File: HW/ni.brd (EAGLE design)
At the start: 122.5 x 35 mm, 71 parts, among them IC1 FAN3100TSX, IC2 STM32G071CBU6, IC3 MIC5504-3.3YM5-TR, Q1 FQD12N20L, Q10 CPH3461, Q11 CPH3461, Q12 CPH3461, Q13 BF821SMD, Q14 CPH3461, Q15 BF821SMD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

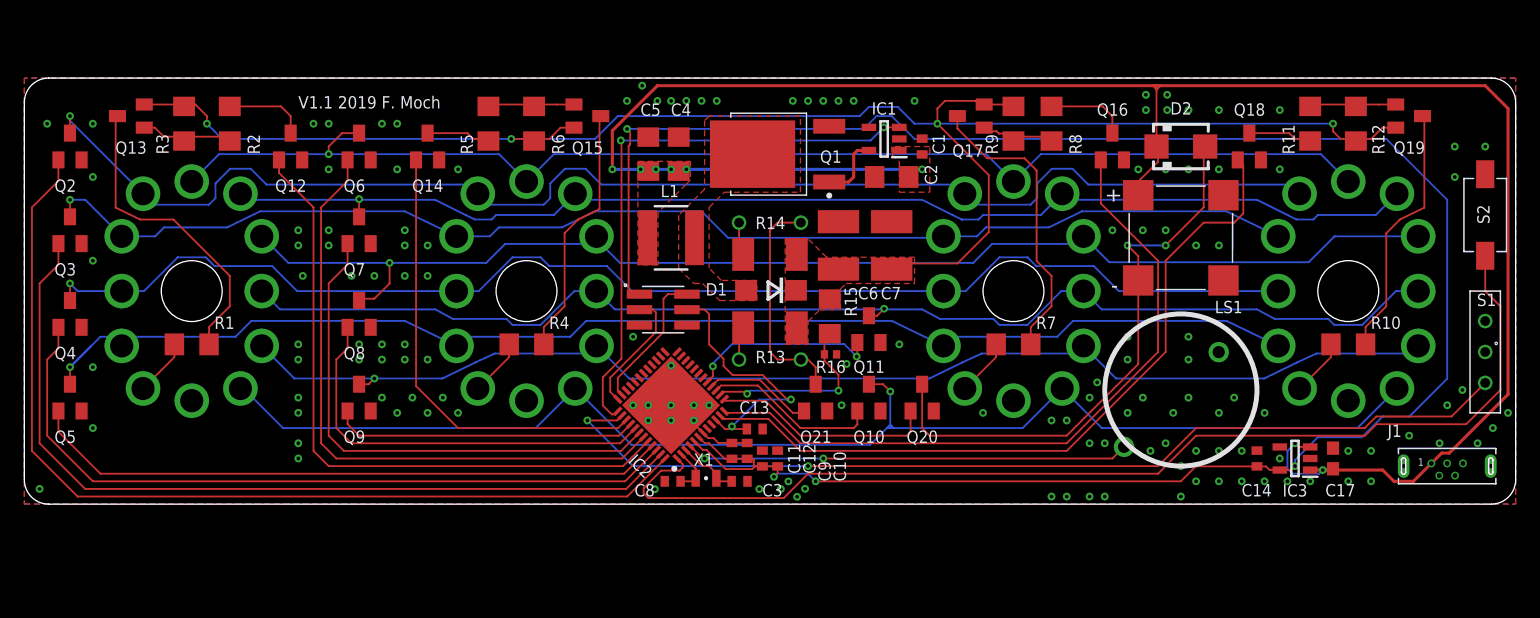
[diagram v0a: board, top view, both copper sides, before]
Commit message: WIFI added
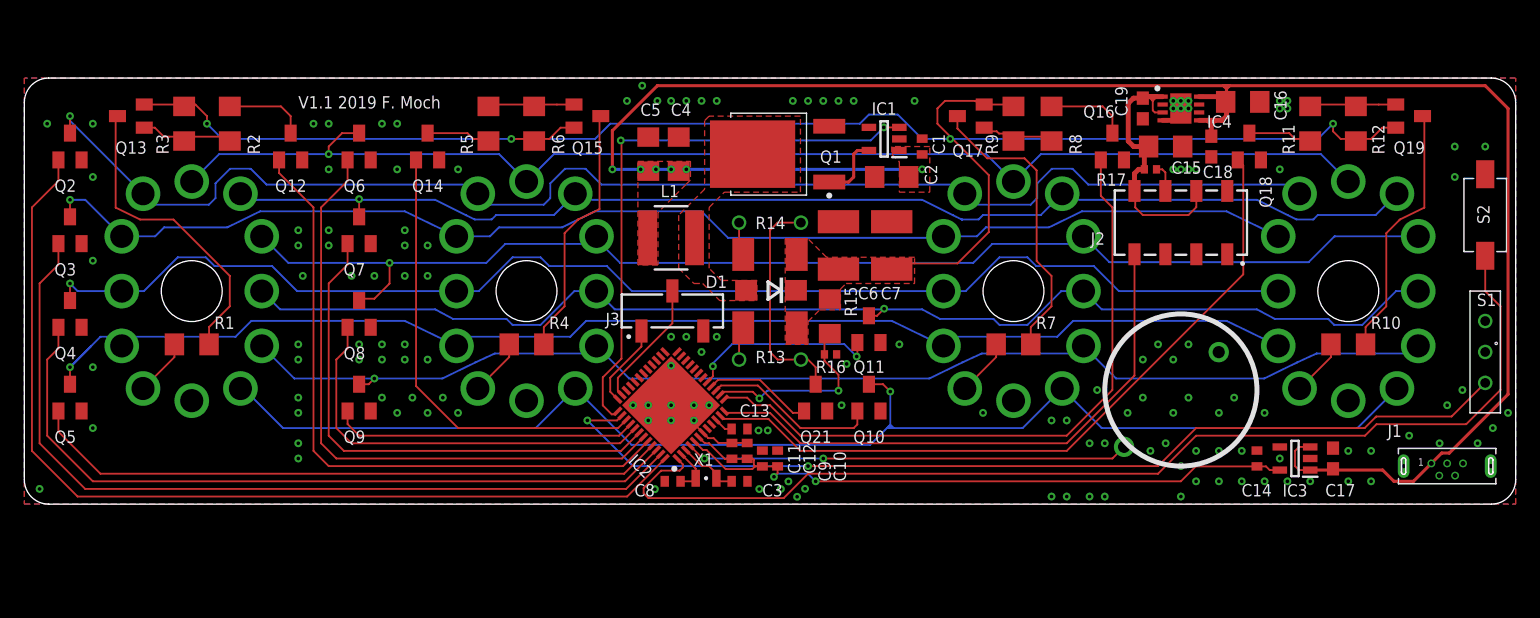
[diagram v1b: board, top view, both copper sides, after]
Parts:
- removed D2: S1M, diode:SMA
- removed LS1: CMT-8540S-SMT, CMT-8540S-SMT:CUI_CMT-8540S-SMT
- removed Q20: 2n7002k, transistor-small-signal:SOT23
- added C15, C16: (no value), rcl:C1206
- added C18, C19: (no value), rcl:C0603
- added IC4: TPS73633DRBR, TPS73633DRBR:SON65P300X300X100-9N
- added J2: (no value), Wurth_Connectors_WR-PHD:61000821821
- added R17: 10k, rcl:R0402
- J3: device EAGLE-BOARD-TO-BOARD_CONNECTORS-rev16c:62100621021 -> OWN_Wurth_Connectors_WR-PHD:OWN-3PIN
- moved J3 2.02 mm to (53.3, 13.4), turned to 180 degrees
- moved C13 1.25 mm to (57.5, 3.67)
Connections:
- removed net LS: IC2.13, Q20.1
- removed net N$34: D2.A, LS1.N, Q20.3
- removed net SWO: J3.4
- new net ESP01: IC2.12, J2.7
- new net N$1: J2.6, R17.2
- new net VCC: C15.1, C19.1, IC4.1, IC4.3, J2.4, J2.8, R17.1
- net +3V3: no longer J3.1
- net +5V: now also C16.2, C18.2, IC4.5, IC4.8; no longer D2.C, LS1.P
- net GN2: now also IC2.13; no longer IC2.12
- net GND: now also C15.2, C16.1, C18.1, C19.2, IC4.4, IC4.9, J2.1; no longer Q20.2
- net NRST: no longer J3.5
- net SWCLK: now also J3.1; no longer J3.2
- net SWDIO: now also J3.2; no longer J3.6
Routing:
- net +3V3: track 174.7 -> 57.7 mm, vias 4 -> 2
- net ESP01: track 0.00 -> 47.0 mm
- net N$34: track 46.8 -> 0.00 mm, vias 2 -> 0
- net VCC: track 0.00 -> 23.6 mm
- net NRST: track 22.4 -> 1.74 mm, vias 2 -> 0
- net LS: track 18.4 -> 0.00 mm
- net +5V: track 166.4 -> 161.6 mm, vias 8 -> 6
- net GN2: track 57.5 -> 54.1 mm
- net SWCLK: track 10.4 -> 6.92 mm
- net N$1: track 0.00 -> 2.35 mm
- net GND: track 7.84 -> 9.49 mm, vias 144 -> 146
- net GN1: track 61.2 -> 59.8 mm
- net SWDIO: track 11.7 -> 10.5 mm
- net V+: track 143.0 -> 143.7 mm

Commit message: ni.brd, ni.sch und 13 weitere dateien aktualisiert...
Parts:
- R1, R10, R4, R7: value 10k -> 15k
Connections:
- net VCC: no longer IC4.3
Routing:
- net VCC: track 23.6 -> 20.9 mm
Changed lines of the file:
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@@
 <attribute name="VALUE" x="10.675" y="27.47" size="1.27" layer="27" rot="R90"/>
 </element>
-<element name="R1" library="rcl" library_urn="urn:adsk.eagle:library:334" package="R1206" package3d_urn="urn:adsk.eagle:package:23540/2" value="10k" x="12.5" y="10.625" smashed="yes">
+<element name="R1" library="rcl" library_urn="urn:adsk.eagle:library:334" package="R1206" package3d_urn="urn:adsk.eagle:package:23540/2" value="15k" x="12.5" y="10.625" smashed="yes">
 <attribute name="NAME" x="14.355" y="11.895" size="1.016" layer="25" font="vector" ratio="10"/>
 <attribute name="POPULARITY" value="41" x="12.5" y="10.625" size="1.778" layer="27" display="off"/>
@@
 <attribute name="VALUE" x="41.825" y="31.28" size="1.27" layer="27" rot="R270"/>
 </element>
-<element name="R4" library="rcl" library_urn="urn:adsk.eagle:library:334" package="R1206" package3d_urn="urn:adsk.eagle:package:23540/2" value="10k" x="40" y="10.625" smashed="yes">
+<element name="R4" library="rcl" library_urn="urn:adsk.eagle:library:334" package="R1206" package3d_urn="urn:adsk.eagle:package:23540/2" value="15k" x="40" y="10.625" smashed="yes">
 <attribute name="NAME" x="41.855" y="11.895" size="1.016" layer="25" font="vector" ratio="10"/>
 <attribute name="POPULARITY" value="41" x="31.875" y="3.125" size="1.778" layer="27" display="off"/>
@@
 <attribute name="VALUE" x="79.669" y="27.47" size="1.27" layer="27" rot="R90"/>
 </element>
-<element name="R7" library="rcl" library_urn="urn:adsk.eagle:library:334" package="R1206" package3d_urn="urn:adsk.eagle:package:23540/2" value="10k" x="80" y="10.625" smashed="yes">
+<element name="R7" library="rcl" library_urn="urn:adsk.eagle:library:334" package="R1206" package3d_urn="urn:adsk.eagle:package:23540/2" value="15k" x="80" y="10.625" smashed="yes">
 <attribute name="NAME" x="81.855" y="11.895" size="1.016" layer="25" font="vector" ratio="10"/>
 <attribute name="POPULARITY" value="41" x="80" y="10.625" size="1.778" layer="27" display="off"/>
@@
 <attribute name="VALUE" x="109.325" y="31.28" size="1.27" layer="27" rot="R270"/>
 </element>
-<element name="R10" library="rcl" library_urn="urn:adsk.eagle:library:334" package="R1206" package3d_urn="urn:adsk.eagle:package:23540/2" value="10k" x="107.5" y="10.625" smashed="yes">
+<element name="R10" library="rcl" library_urn="urn:adsk.eagle:library:334" package="R1206" package3d_urn="urn:adsk.eagle:package:23540/2" value="15k" x="107.5" y="10.625" smashed="yes">
 <attribute name="NAME" x="109.355" y="11.895" size="1.016" layer="25" font="vector" ratio="10"/>
 <attribute name="POPULARITY" value="41" x="107.5" y="10.625" size="1.778" layer="27" display="off"/>
@@
 <signal name="VCC">
 <contactref element="IC4" pad="1"/>
-<contactref element="IC4" pad="3"/>
 <contactref element="R17" pad="1"/>
 <contactref element="J2" pad="8"/>
@@
 <contactref element="C19" pad="1"/>
 <wire x1="92.25" y1="30.975" x2="91.694" y2="30.975" width="0.4064" layer="1"/>
-<wire x1="91.694" y1="30.975" x2="91.44" y2="30.975" width="0.4064" layer="1"/>
-<wire x1="91.44" y1="30.975" x2="91.186" y2="30.975" width="0.4064" layer="1"/>
+<wire x1="91.694" y1="30.975" x2="91.186" y2="30.975" width="0.4064" layer="1"/>
 <wire x1="90.75" y1="30.975" x2="91.186" y2="30.975" width="0.4064" layer="1"/>
 <wire x1="90.75" y1="30.975" x2="90.625" y2="30.85" width="0.4064" layer="1"/>
@@
 <wire x1="89.4282" y1="27.3198" x2="89.873" y2="26.875" width="0.4064" layer="1"/>
 <wire x1="89.873" y1="26.875" x2="91.1" y2="26.875" width="0.4064" layer="1"/>
-<wire x1="92.25" y1="29.675" x2="91.61" y2="29.675" width="0.1524" layer="1"/>
-<wire x1="91.61" y1="29.675" x2="91.44" y2="29.845" width="0.1524" layer="1"/>
-<wire x1="91.44" y1="29.845" x2="91.44" y2="30.625" width="0.1524" layer="1"/>
-<wire x1="91.44" y1="30.975" x2="91.44" y2="30.625" width="0.1524" layer="1"/>
-<wire x1="91.44" y1="30.625" x2="91.186" y2="30.879" width="0.1524" layer="1"/>
 <wire x1="91.186" y1="30.879" x2="91.186" y2="30.975" width="0.1524" layer="1"/>
-<wire x1="91.44" y1="30.625" x2="91.694" y2="30.879" width="0.1524" layer="1"/>
 <wire x1="91.694" y1="30.879" x2="91.694" y2="30.975" width="0.1524" layer="1"/>
 </signal>

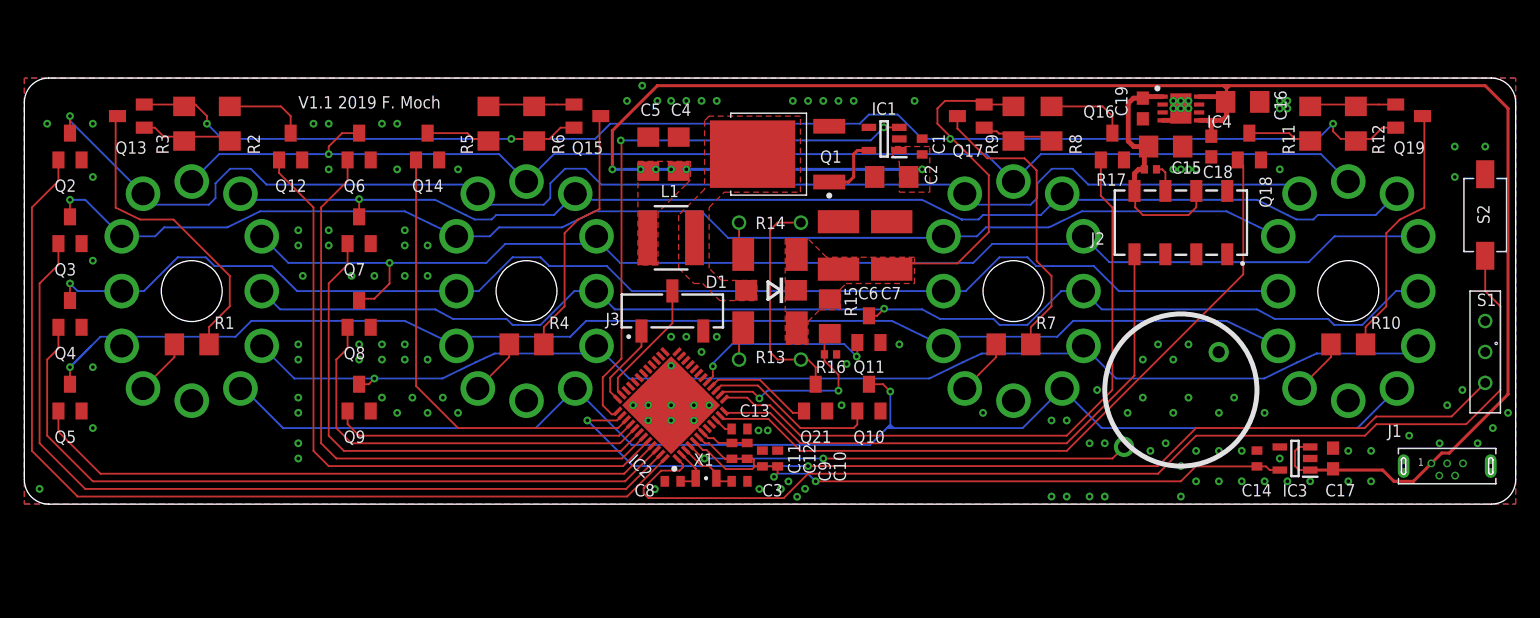
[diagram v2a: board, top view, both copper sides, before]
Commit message: working on snubber design
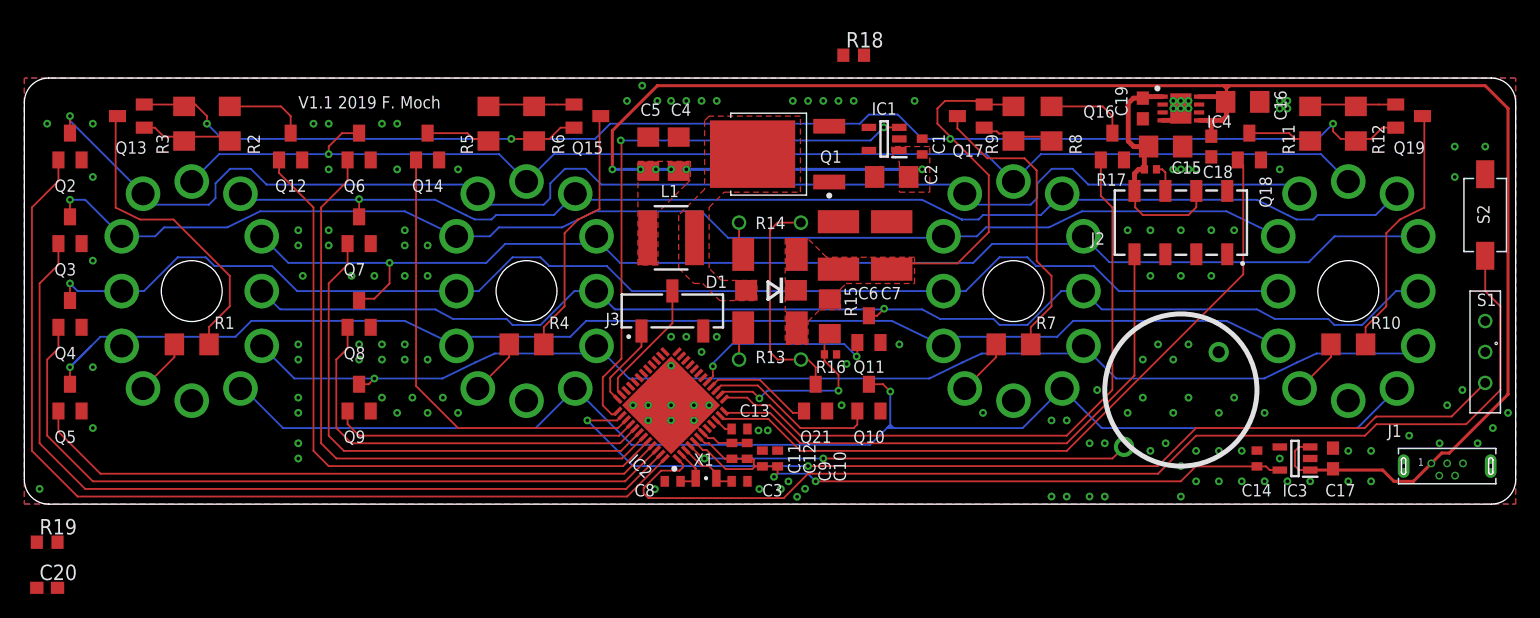
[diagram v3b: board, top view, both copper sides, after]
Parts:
- added C20: (no value), rcl:C0603
- added R18: 7.5, rcl:R0603
- added R19: (no value), rcl:R0603
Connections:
- new net N$18: IC1.5, R18.1
- new net N$25: C20.2, R19.2
- net GND: now also R19.1
- net N$2: now also C20.1
- net N$3: now also R18.2; no longer IC1.5
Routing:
- net N$3: track 5.43 -> 0.00 mm
- net GND: vias 146 -> 154
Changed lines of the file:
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@@
 <?xml version="1.0" encoding="utf-8"?>
 <!DOCTYPE eagle SYSTEM "eagle.dtd">
-<eagle version="9.5.2">
+<eagle version="9.6.2">
 <drawing>
 <settings>
-<setting alwaysvectorfont="no"/>
+<setting alwaysvectorfont="yes"/>
 <setting verticaltext="up"/>
 </settings>
@@
 </layers>
 <board>
-<fusionsync huburn="a.cGVyc29uYWw6dWUyYTQ0OWEy" projecturn="a.cGVyc29uYWw6dWUyYTUyZDdlIzIwMTgwMTIyMTEzNTIxMjAx" f3durn="urn:adsk.wipprod:dm.lineage:zjynMPhCQdOZMy_LPZ6NnQ" pcbguid="72f60802-4ef6-4f0b-8764-49804ee53bed" lastpulledtime="" lastsyncedchangeguid="45c9e04f-f793-9a3e-dfb9-808f387d40d0"/>
+<fusionsync huburn="a.cGVyc29uYWw6dWUyYTQ0OWEy" projecturn="a.cGVyc29uYWw6dWUyYTUyZDdlIzIwMTgwMTIyMTEzNTIxMjAx" f3durn="urn:adsk.wipprod:dm.lineage:zjynMPhCQdOZMy_LPZ6NnQ" pcbguid="72f60802-4ef6-4f0b-8764-49804ee53bed" lastpulledtime="" lastsyncedchangeguid="45c9e04f-f793-9a3e-dfb9-808f387d40d0" latestrevisionid="" lastsyncedrevisionid="" lastboardhashguid="" lastpushedtime="" linktopcb3d="false"/>
 <plain>
 <wire x1="-1.25" y1="30.5" x2="-1.25" y2="-0.5" width="0" layer="20"/>
@@
 <attribute name="VALUE" x="46.8132" y="14.6896" size="1.016" layer="27" rot="R180"/>
 </element>
+<element name="R18" library="rcl" library_urn="urn:adsk.eagle:library:334" package="R0603" package3d_urn="urn:adsk.eagle:package:23555/3" value="7.5" x="66.875" y="34.375" smashed="yes">
+<attribute name="NAME" x="66.24" y="35.01" size="1.27" layer="25"/>
+<attribute name="POPULARITY" value="70" x="66.875" y="34.375" size="1.778" layer="27" display="off"/>
+<attribute name="SPICEPREFIX" value="R" x="66.875" y="34.375" size="1.778" layer="27" display="off"/>
+<attribute name="VALUE" x="66.24" y="32.47" size="1.27" layer="27"/>
+</element>
+<element name="R19" library="rcl" library_urn="urn:adsk.eagle:library:334" package="R0603" package3d_urn="urn:adsk.eagle:package:23555/3" value="" x="0.625" y="-5.625" smashed="yes">
+<attribute name="NAME" x="-0.01" y="-4.99" size="1.27" layer="25"/>
+<attribute name="POPULARITY" value="70" x="0.625" y="-5.625" size="1.778" layer="27" display="off"/>
+<attribute name="SPICEPREFIX" value="R" x="0.625" y="-5.625" size="1.778" layer="27" display="off"/>
+<attribute name="VALUE" x="-0.01" y="-7.53" size="1.27" layer="27"/>
+</element>
+<element name="C20" library="rcl" library_urn="urn:adsk.eagle:library:334" package="C0603" package3d_urn="urn:adsk.eagle:package:23616/2" value="" x="0.625" y="-9.375" smashed="yes">
+<attribute name="NAME" x="-0.01" y="-8.74" size="1.27" layer="25"/>
+<attribute name="POPULARITY" value="73" x="0.625" y="-9.375" size="1.778" layer="27" display="off"/>
+<attribute name="SPICEPREFIX" value="C" x="0.625" y="-9.375" size="1.778" layer="27" display="off"/>
+<attribute name="VALUE" x="-0.01" y="-11.28" size="1.27" layer="27"/>
+</element>
 </elements>
 <signals>
@@
 <vertex x="55.869" y="14.224"/>
 </polygon>
+<contactref element="C20" pad="1"/>
+<wire x1="53.8" y1="19.375" x2="-0.225" y2="-9.375" width="0" layer="19" extent="1-1"/>
 </signal>
 <signal name="GND">
@@
 <via x="51.875" y="11.25" extent="1-16" drill="0.3" diameter="0.65"/>
 <via x="55.625" y="11.25" extent="1-16" drill="0.3" diameter="0.65"/>
-</signal>
-<signal name="N$3">
-<contactref element="IC1" pad="5"/>
-<contactref element="Q1" pad="1"/>
-<wire x1="68.125" y1="26.55" x2="67.175" y2="26.55" width="0.254" layer="1"/>
-<wire x1="67.175" y1="26.55" x2="66.875" y2="26.25" width="0.254" layer="1"/>
-<wire x1="66.875" y1="26.25" x2="66.875" y2="24.375" width="0.254" layer="1"/>
-<wire x1="66.875" y1="24.375" x2="66.46" y2="23.96" width="0.254" layer="1"/>
-<wire x1="66.46" y1="23.96" x2="64.8659" y2="23.96" width="0.254" layer="1"/>
+<via x="91.25" y="16.25" extent="1-16" drill="0.3" diameter="0.65"/>
+<via x="93.75" y="16.25" extent="1-16" drill="0.3" diameter="0.65"/>
+<via x="96.25" y="16.25" extent="1-16" drill="0.3" diameter="0.65"/>
+<via x="91.25" y="20" extent="1-16" drill="0.3" diameter="0.65"/>
+<via x="89.375" y="20" extent="1-16" drill="0.3" diameter="0.65"/>
+<via x="93.75" y="20" extent="1-16" drill="0.3" diameter="0.65"/>
+<via x="96.25" y="20" extent="1-16" drill="0.3" diameter="0.65"/>
+<via x="98.125" y="20" extent="1-16" drill="0.3" diameter="0.65"/>
+<contactref element="R19" pad="1"/>
+<wire x1="0" y1="-1.25" x2="-0.225" y2="-5.625" width="0" layer="19" extent="1-1"/>
 </signal>
 <signal name="+5V">
@@
 <wire x1="84.375" y1="2.5" x2="89.94" y2="8.065" width="0.1524" layer="1"/>
 </signal>
+<signal name="N$3">
+<contactref element="Q1" pad="1"/>
+<contactref element="R18" pad="2"/>
+<wire x1="67.725" y1="34.375" x2="64.8659" y2="23.96" width="0" layer="19" extent="1-1"/>
+</signal>
+<signal name="N$18">
+<contactref element="R18" pad="1"/>
+<contactref element="IC1" pad="5"/>
+<wire x1="66.025" y1="34.375" x2="68.125" y2="26.55" width="0" layer="19" extent="1-1"/>
+</signal>
+<signal name="N$25">
+<contactref element="C20" pad="2"/>
+<contactref element="R19" pad="2"/>
+<wire x1="1.475" y1="-5.625" x2="1.475" y2="-9.375" width="0" layer="19" extent="1-1"/>
+</signal>
 </signals>

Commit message: rc snubber
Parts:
- C20: device rcl:C0603 -> rcl:C1206
- R19: device rcl:R0603 -> rcl:R1206
- moved R19 69.9 mm to (64.4, 23.1), turned to 180 degrees
- moved C20 66.6 mm to (58.8, 23.1)
- moved R18 6.90 mm to (67.5, 27.5), turned to 90 degrees
- moved Q1 1.88 mm to (60.6, 28.1)
- moved C2 1.25 mm to (70.0, 23.1)
- moved IC1 1.25 mm to (70.6, 27.5)
- moved C4 1.02 mm to (51.5, 26.2)
- moved C1 0.91 mm to (73.4, 26.6)
- moved C5 0.62 mm to (49.4, 26.2)
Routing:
- net N$3: track 0.00 -> 4.57 mm
- net N$18: track 0.00 -> 1.99 mm
- net GND: track 9.49 -> 10.9 mm, vias 154 -> 151
- net PWM+: track 47.4 -> 48.6 mm
- net +5V: track 161.6 -> 161.8 mm, vias 6 -> 4
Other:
- board text added: "V1.2 2021 F. Moch"
- board text removed: "V1.1 2019 F. Moch"
